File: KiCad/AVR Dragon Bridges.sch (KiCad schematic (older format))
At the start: 5 parts

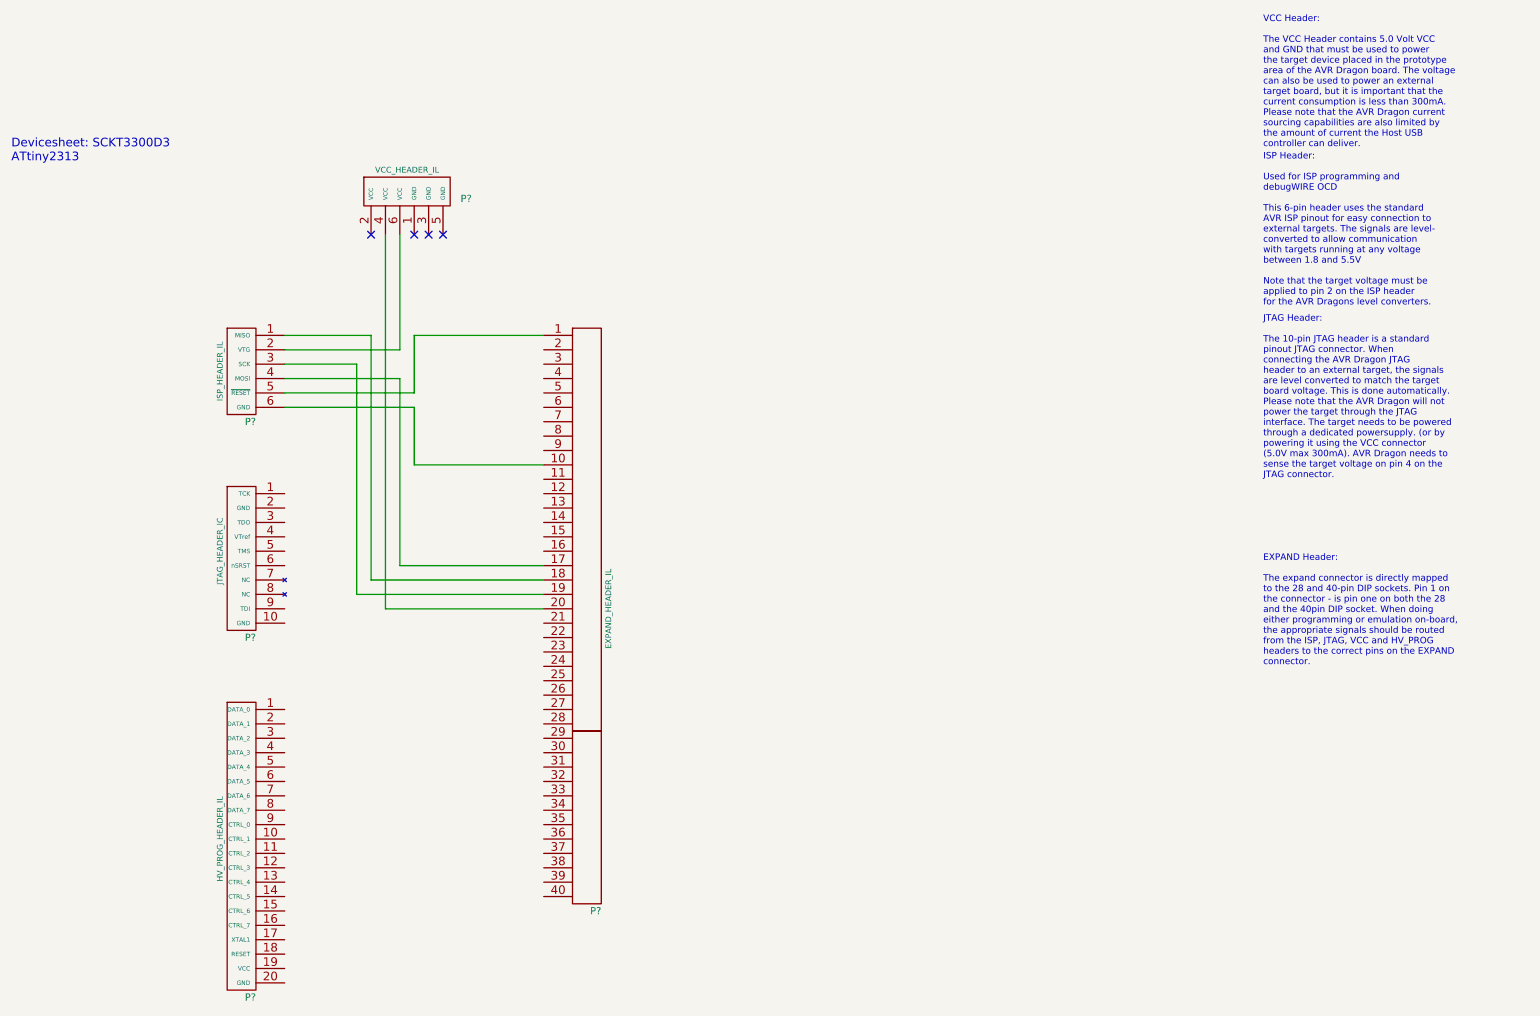
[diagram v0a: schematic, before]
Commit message: Completed preliminary PCB for ATtiny2313. Tidied up some schematics.
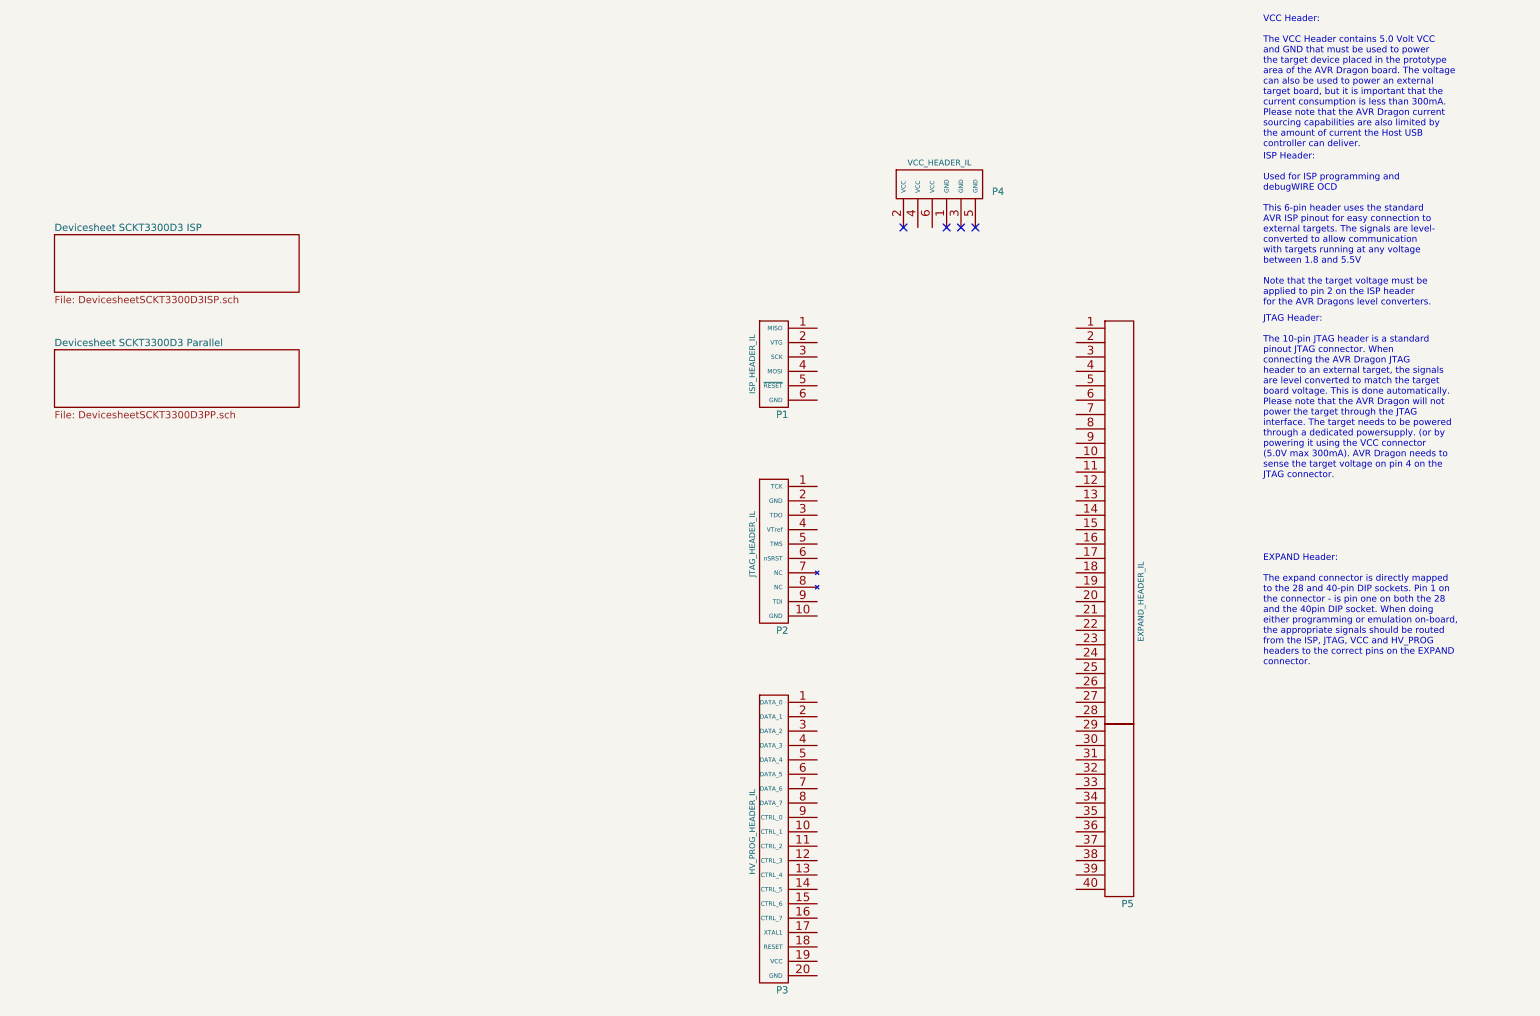
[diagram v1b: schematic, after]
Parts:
- removed P?: JTAG_HEADER_IC, symbol JTAG_HEADER_IC
- added P2: JTAG_HEADER_IL, ~, symbol JTAG_HEADER_IL
- gave numbers to parts that had none: 4
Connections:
- net at P5.1: no longer P1.5 (~RESET)
- net at P5.10: no longer P1.6 (GND)
- net at P5.17: no longer P1.4 (MOSI)
- net at P5.18: no longer P1.1 (MISO)
- net at P5.19: no longer P1.3 (SCK)
- net at P5.20: no longer P4.4 (VCC)
- net at P1.2 (VTG): no longer P4.6 (VCC)
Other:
- note removed: "Devicesheet: SCKT3300D3\nATtiny2313"
- moved on the sheet: P1, P3, P4, P5
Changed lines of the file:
@@
 $Descr A4 11693 8268
 encoding utf-8
-Sheet 1 1
+Sheet 1 3
 Title "AVR Dragon Bridges"
 Date "28 apr 2014"
@@
 EXPAND Header:\n\nThe expand connector is directly mapped\nto the 28 and 40-pin DIP sockets. Pin 1 on\nthe connector - is pin one on both the 28\nand the 40pin DIP socket. When doing\neither programming or emulation on-board,\nthe appropriate signals should be routed\nfrom the ISP, JTAG, VCC and HV_PROG\nheaders to the correct pins on the EXPAND\nconnector.
 $Comp
-L EXPAND_HEADER_IL P?
+L EXPAND_HEADER_IL P5
 U 1 1 535E21DF
-P 4900 3900
-F 0 "P?" H 4900 1800 50  0000 R CNN
-F 1 "EXPAND_HEADER_IL" V 4950 3900 40  0000 C CNN
-F 2 "" H 4900 5650 60  0000 C CNN
-F 3 "" H 4900 5650 60  0000 C CNN
-	1    4900 3900
+P 8600 3850
+F 0 "P5" H 8600 1750 50  0000 R CNN
+F 1 "EXPAND_HEADER_IL" V 8650 3850 40  0000 C CNN
+F 2 "" H 8600 5600 60  0000 C CNN
+F 3 "" H 8600 5600 60  0000 C CNN
+	1    8600 3850
 	1    0    0    -1
 $EndComp
 $Comp
-L ISP_HEADER_IL P?
+L ISP_HEADER_IL P1
 U 1 1 535E21EE
-P 2300 2200
-F 0 "P?" H 2500 1800 50  0000 R CNN
-F 1 "ISP_HEADER_IL" V 2250 2150 40  0000 C CNN
-F 2 "" H 2300 2250 60  0000 C CNN
-F 3 "" H 2300 2250 60  0000 C CNN
-	1    2300 2200
+P 6000 2150
+F 0 "P1" H 6200 1750 50  0000 R CNN
+F 1 "ISP_HEADER_IL" V 5950 2100 40  0000 C CNN
+F 2 "" H 6000 2200 60  0000 C CNN
+F 3 "" H 6000 2200 60  0000 C CNN
+	1    6000 2150
 	1    0    0    -1
 $EndComp
 $Comp
-L JTAG_HEADER_IC P?
-U 1 1 535E220C
-P 2300 3500
-F 0 "P?" H 2500 2900 50  0000 R CNN
-F 1 "JTAG_HEADER_IC" V 2250 3500 40  0000 C CNN
-F 2 "" H 2300 3750 60  0000 C CNN
-F 3 "" H 2300 3750 60  0000 C CNN
-	1    2300 3500
+L HV_PROG_HEADER_IL P3
+U 1 1 535E221B
+P 6000 5450
+F 0 "P3" H 6200 4350 50  0000 R CNN
+F 1 "HV_PROG_HEADER_IL" V 5950 5450 40  0000 C CNN
+F 2 "" H 6000 6200 60  0000 C CNN
+F 3 "" H 6000 6200 60  0000 C CNN
+	1    6000 5450
 	1    0    0    -1
 $EndComp
 $Comp
-L HV_PROG_HEADER_IL P?
-U 1 1 535E221B
-P 2300 5500
-F 0 "P?" H 2500 4400 50  0000 R CNN
-F 1 "HV_PROG_HEADER_IL" V 2250 5500 40  0000 C CNN
-F 2 "" H 2300 6250 60  0000 C CNN
-F 3 "" H 2300 6250 60  0000 C CNN
-	1    2300 5500
+L VCC_HEADER_IL P4
+U 1 1 535E222A
+P 7200 850
+F 0 "P4" H 7700 700 50  0000 R CNN
+F 1 "VCC_HEADER_IL" H 7250 900 40  0000 C CNN
+F 2 "" V 7250 850 60  0000 C CNN
+F 3 "" V 7250 850 60  0000 C CNN
+	1    7200 850
 	1    0    0    -1
 $EndComp
+NoConn ~ 7000 1250
+NoConn ~ 7300 1250
+NoConn ~ 7400 1250
+NoConn ~ 7500 1250
 $Comp
-L VCC_HEADER_IL P?
-U 1 1 535E222A
-P 3500 900
-F 0 "P?" H 4000 750 50  0000 R CNN
-F 1 "VCC_HEADER_IL" H 3550 950 40  0000 C CNN
-F 2 "" V 3550 900 60  0000 C CNN
-F 3 "" V 3550 900 60  0000 C CNN
-	1    3500 900
+L JTAG_HEADER_IL P2
+U 1 1 535E1EAE
+P 6000 3450
+F 0 "P2" H 6200 2850 50  0000 R CNN
+F 1 "JTAG_HEADER_IL" V 5950 3450 40  0000 C CNN
+F 2 "~" H 6000 3700 60  0000 C CNN
+F 3 "~" H 6000 3700 60  0000 C CNN
+	1    6000 3450
 	1    0    0    -1
 $EndComp
-Wire Wire Line
-	3500 2100 2700 2100
-Wire Wire Line
-	3500 1300 3500 2100
-Wire Wire Line
-	3400 1300 3400 3900
-Wire Wire Line
-	3400 3900 4500 3900
-Wire Wire Line
-	2700 2000 3300 2000
-Wire Wire Line
-	3300 2000 3300 3700
-Wire Wire Line
-	3300 3700 4500 3700
-Wire Wire Line
-	2700 2200 3200 2200
-Wire Wire Line
-	3200 2200 3200 3800
-Wire Wire Line
-	3200 3800 4500 3800
-Wire Wire Line
-	2700 2300 3500 2300
-Wire Wire Line
-	3500 2300 3500 3600
-Wire Wire Line
-	3500 3600 4500 3600
-Wire Wire Line
-	2700 2400 3600 2400
-Wire Wire Line
-	3600 2400 3600 2000
-Wire Wire Line
-	3600 2000 4500 2000
-Wire Wire Line
-	2700 2500 3600 2500
-Wire Wire Line
-	3600 2500 3600 2900
-Wire Wire Line
-	3600 2900 4500 2900
-NoConn ~ 3300 1300
-NoConn ~ 3600 1300
-NoConn ~ 3700 1300
-NoConn ~ 3800 1300
-Text Notes 800  800  0    60   ~ 0
-Devicesheet: SCKT3300D3\nATtiny2313
+$Sheet
+S 1100 1300 1700 400
+U 535E2066
+F0 "Devicesheet SCKT3300D3 ISP" 50
+F1 "DevicesheetSCKT3300D3ISP.sch" 50
+$EndSheet
+$Sheet
+S 1100 2100 1700 400
+U 535E21B4
+F0 "Devicesheet SCKT3300D3 Parallel" 50
+F1 "DevicesheetSCKT3300D3PP.sch" 50
+$EndSheet
 $EndSCHEMATC
